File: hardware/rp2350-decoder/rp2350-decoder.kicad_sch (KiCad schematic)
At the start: 67 parts, among them J1 SWDIO, J2 SWCLK, J3 5052702412, Q1 DMN2991UDA-7B, Q2 DMN2991UDA-7B, Q3 NST847BPDP6T5G, Q4 NST847BPDP6T5G, Q5 DMN2991UDA-7B, Q6 DMN2991UDA-7B, Q7 DMN2991UDA-7B, Q8 DMN2991UDA-7B, SW1 BOOT, U1 NCS2220AMUT1G, U2 AP63203WU, U3 W25Q128JVPIQ, U4 RP2350A, U5 MAX98357AEWL+T, U6 MD9927, Y1 X252012MMB4SI

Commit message: chore: pcb cleanup
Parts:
- C2: Height 1.0 -> 0.9
- Y1: Frequency 12MHz -> (none)
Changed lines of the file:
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@@
 			)
 		)
-		(property "Datasheet" "https://lcsc.com/product-detail/Motor-Drivers_Shanghai-Mingda-Microelectronics-MD9927_C2684662.html"
+		(property "Datasheet" "https://www.lcsc.com/datasheet/lcsc_datasheet_2101111937_Shanghai-Mingda-Microelectronics-MD9927_C2684662.pdf"
 			(at 355.346 235.458 0)
 			(effects
@@
 			)
 		)
-		(property "Frequency" "12MHz"
-			(at 123.952 161.29 0)
-			(effects
-				(font
-					(size 1.27 1.27)
-				)
-			)
-		)
 		(pin "2"
 		)
@@
 			)
 		)
-		(property "Height" "1.0"
+		(property "Height" "0.9"
 			(at 74.93 54.61 0)
 			(effects

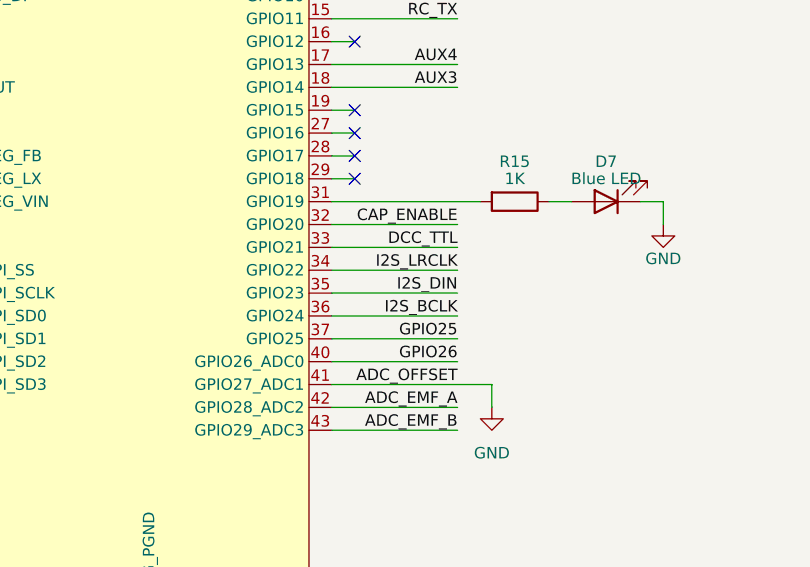
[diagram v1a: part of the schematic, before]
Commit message: chore: rearrange i2s pins for easier pio use
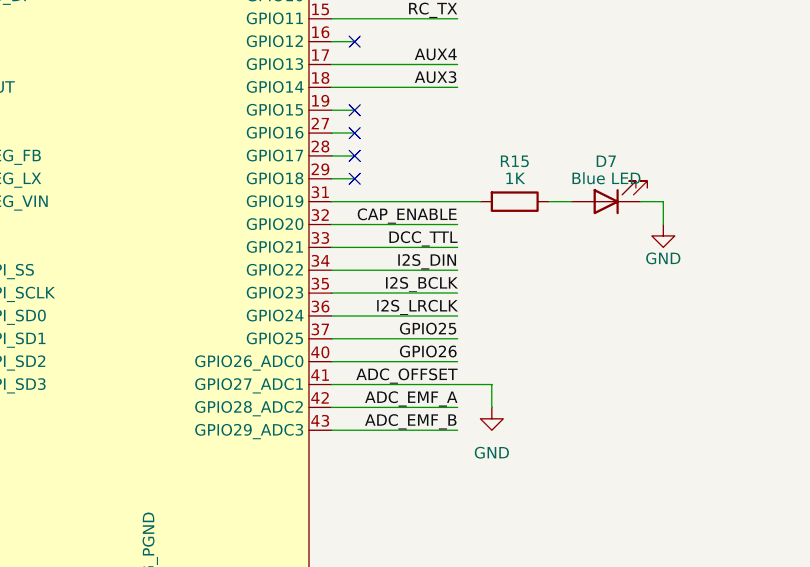
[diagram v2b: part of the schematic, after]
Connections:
- net I2S_BCLK: now also U4.35 (GPIO23); no longer U4.36 (GPIO24)
- net I2S_DIN: now also U4.34 (GPIO22); no longer U4.35 (GPIO23)
- net I2S_LRCLK: now also U4.36 (GPIO24); no longer U4.34 (GPIO22)
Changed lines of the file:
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@@
 	)
 	(label "I2S_BCLK"
-		(at 246.38 219.71 180)
+		(at 246.38 217.17 180)
 		(effects
 			(font
@@
 	)
 	(label "I2S_DIN"
-		(at 246.38 217.17 180)
+		(at 246.38 214.63 180)
 		(effects
 			(font
@@
 	)
 	(label "I2S_LRCLK"
-		(at 246.38 214.63 180)
-		(effects
-			(font
+		(at 246.38 219.71 180)
+		(effects
+			(font

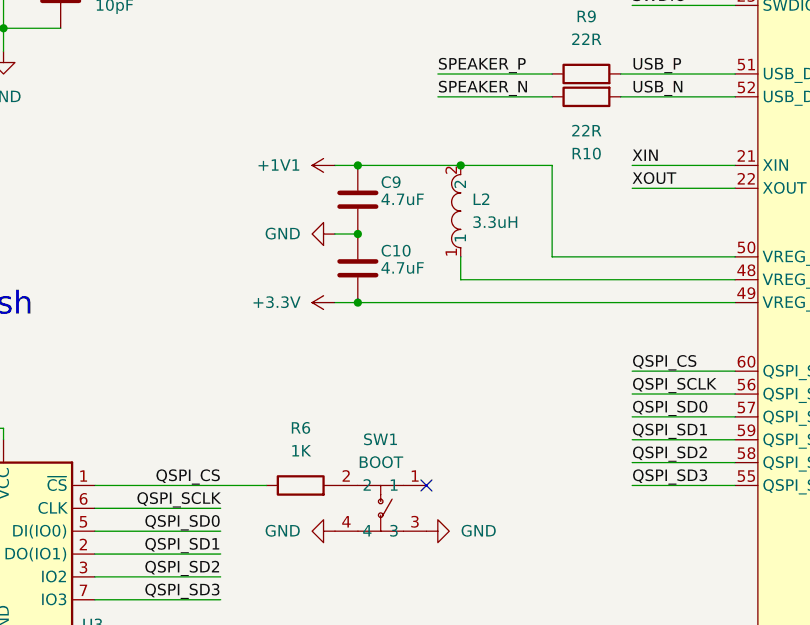
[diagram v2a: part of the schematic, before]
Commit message: chore: increase bootsel resistance
chore: add missing heights
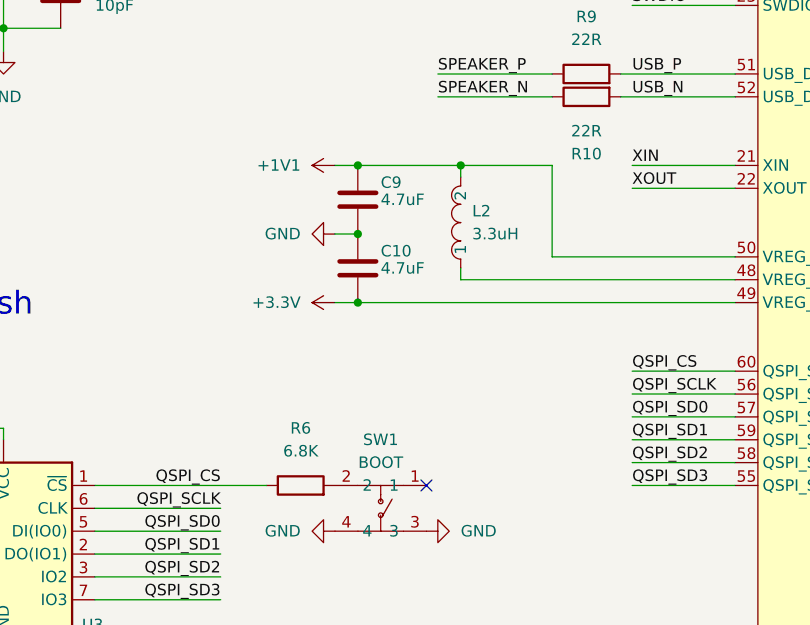
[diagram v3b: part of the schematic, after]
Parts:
- C14: Height 0.7 -> 0.55
- J1, J2: Height (none) -> 0
- L2: Height (none) -> 1.0; LCSC Part (none) -> C42411119
- Q3, Q4: Height (none) -> 0.4
- R10, R11, R13, R14, R5, R9: Height (none) -> 0.26
- R6: value 1K -> 6.8K; LCSC C270365 -> C423451
- U4: Height (none) -> 0.9
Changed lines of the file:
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@@
 	(wire
 		(pts
-			(xy 158.75 201.93) (xy 158.75 204.47)
+			(xy 158.75 203.2) (xy 158.75 204.47)
 		)
 		(stroke
@@
 	(wire
 		(pts
+			(xy 158.75 193.04) (xy 158.75 191.77)
+		)
+		(stroke
+			(width 0)
+			(type default)
+		)
+	)
+	(wire
+		(pts
 			(xy 232.41 204.47) (xy 234.95 204.47)
 		)
@@
 			)
 		)
+		(property "Height" "0.4"
+			(at 215.9 48.26 0)
+			(effects
+				(font
+					(size 1.27 1.27)
+				)
+				(hide yes)
+			)
+		)
 		(pin "2"
 		)
@@
 			)
 		)
+		(property "Height" "0.26"
+			(at 224.79 57.15 0)
+			(effects
+				(font
+					(size 1.27 1.27)
+				)
+				(hide yes)
+			)
+		)
 		(pin "1"
 		)
@@
 			)
 		)
+		(property "Height" "0.26"
+			(at 96.52 167.64 0)
+			(effects
+				(font
+					(size 1.27 1.27)
+				)
+				(hide yes)
+			)
+		)
 		(pin "1"
 		)
@@
 			)
 		)
+		(property "Height" "0.4"
+			(at 201.93 76.2 0)
+			(effects
+				(font
+					(size 1.27 1.27)
+				)
+				(hide yes)
+			)
+		)
 		(pin "2"
 		)
@@
 			)
 		)
+		(property "Height" "0.26"
+			(at 172.72 181.61 0)
+			(effects
+				(font
+					(size 1.27 1.27)
+				)
+				(hide yes)
+			)
+		)
 		(pin "2"
 		)
@@
 	(symbol
 		(lib_id "rp2350-decoder:AOTA-B201610S3R3-101-T")
-		(at 158.75 196.85 90)
+		(at 158.75 198.12 90)
 		(unit 1)
 		(exclude_from_sim no)
@@
 		(fields_autoplaced yes)
 		(property "Reference" "L2"
-			(at 160.02 195.5799 90)
+			(at 160.02 196.8499 90)
 			(effects
 				(font
@@
 		)
 		(property "Value" "3.3uH"
-			(at 160.02 198.1199 90)
+			(at 160.02 199.3899 90)
 			(effects
 				(font
@@
 		)
 		(property "Footprint" "rp2350-decoder:IND-SMD_L2.0-W1.6_AOTA-B201610S3R3-101-T"
-			(at 166.37 196.85 0)
+			(at 166.37 198.12 0)
 			(effects
 				(font
@@
 		)
 		(property "Datasheet" "https://jlcpcb.com/api/file/downloadByFileSystemAccessId/8567843503118221312"
-			(at 158.75 196.85 0)
+			(at 158.75 198.12 0)
 			(effects
 				(font
@@
 		)
 		(property "Description" ""
-			(at 158.75 196.85 0)
+			(at 158.75 198.12 0)
 			(effects
 				(font
@@
 		)
 		(property "LCSC" "C42411119"
-			(at 168.91 196.85 0)
+			(at 168.91 198.12 0)
+			(effects
+				(font
+					(size 1.27 1.27)
+				)
+				(hide yes)
+			)
+		)
+		(property "Height" "1.0"
+			(at 158.75 198.12 0)
+			(effects
+				(font
+					(size 1.27 1.27)
+				)
+				(hide yes)
+			)
+		)
+		(property "LCSC Part" "C42411119"
+			(at 168.91 198.12 0)
 			(effects
 				(font
@@
 			)
 		)
-		(property "Value" "1K"
+		(property "Value" "6.8K"
 			(at 140.97 223.52 90)
 			(effects
@@
 			)
 		)
-		(property "LCSC" "C270365"
+		(property "LCSC" "C423451"
 			(at 140.97 227.33 0)
 			(effects
@@
 			)
 		)
+		(property "Height" "0"
+			(at 160.02 154.94 0)
+			(effects
+				(font
+					(size 1.27 1.27)
+				)
+				(hide yes)
+			)
+		)
 		(pin "1"
 		)
@@
 			)
 		)
-		(property "Height" "0.7"
+		(property "Height" "0.55"
 			(at 236.22 140.97 0)
 			(effects
@@
 			)
 		)
+		(property "Height" "0.4"
+			(at 209.55 57.15 0)
+			(effects
+				(font
+					(size 1.27 1.27)
+				)
+				(hide yes)
+			)
+		)
 		(pin "2"
 		)
@@
 			)
 		)
+		(property "Height" "0.26"
+			(at 207.01 44.45 0)
+			(effects
+				(font
+					(size 1.27 1.27)
+				)
+				(hide yes)
+			)
+		)
 		(pin "2"
 		)
@@
 			)
 		)
+		(property "Height" "0.4"
+			(at 219.71 76.2 0)
+			(effects
+				(font
+					(size 1.27 1.27)
+				)
+				(hide yes)
+			)
+		)
 		(pin "2"
 		)
@@
 			)
 		)
+		(property "Height" "0.26"
+			(at 172.72 184.15 0)
+			(effects
+				(font
+					(size 1.27 1.27)
+				)
+				(hide yes)
+			)
+		)
 		(pin "2"
 		)
@@
 			)
 		)
+		(property "Height" "0"
+			(at 160.02 160.02 0)
+			(effects
+				(font
+					(size 1.27 1.27)
+				)
+				(hide yes)
+			)
+		)
 		(pin "1"
 		)
@@
 			)
 		)
+		(property "Height" "0.26"
+			(at 246.38 134.62 0)
+			(effects
+				(font
+					(size 1.27 1.27)
+				)
+				(hide yes)
+			)
+		)
 		(pin "2"
 		)
@@
 			(effects
 				(font
+					(size 1.27 1.27)
+				)
+				(hide yes)
+			)
+		)
+		(property "Height" "0.9"
+			(at 210.82 195.58 0)
+			(effects
+				(font

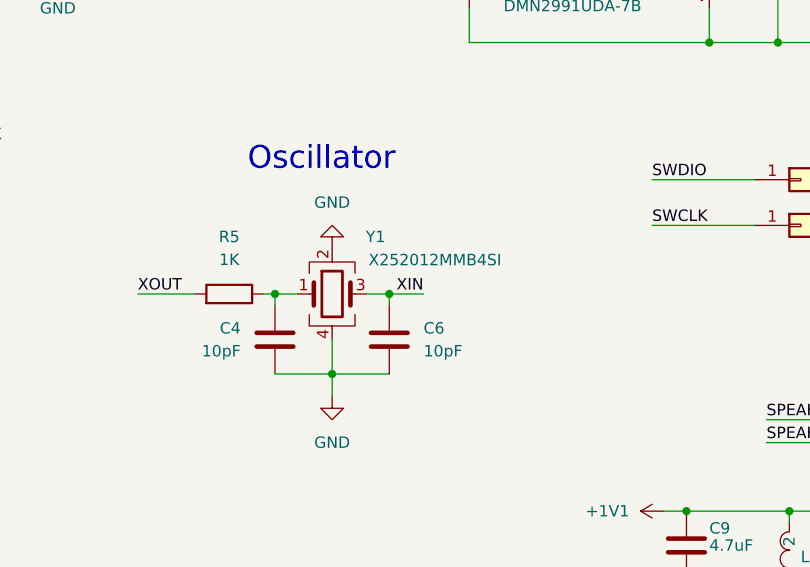
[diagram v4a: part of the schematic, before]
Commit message: fix: switch to recommended crystal
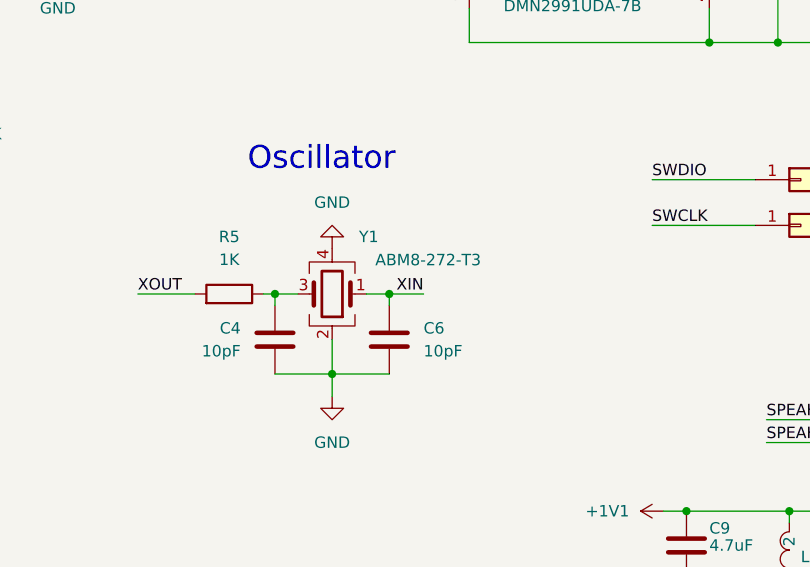
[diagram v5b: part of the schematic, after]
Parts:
- Y1: value X252012MMB4SI -> ABM8-272-T3; footprint Crystal:Crystal_SMD_2520-4Pin_2.5x2.0mm -> Crystal:Crystal_SMD_3225-4Pin_3.2x2.5mm; Height 0.65 -> 0.8; LCSC C2896601 -> C20625731
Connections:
- net XIN: now also Y1.1; no longer Y1.3
- net at C4.1, R5.1: now also Y1.3; no longer Y1.1
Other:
- moved on the sheet: Y1
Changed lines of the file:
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@@
 	(symbol
 		(lib_id "Device:Crystal_GND24")
-		(at 107.95 167.64 0)
+		(at 107.95 167.64 180)
 		(unit 1)
 		(exclude_from_sim no)
@@
 		(dnp no)
 		(property "Reference" "Y1"
-			(at 112.776 161.29 0)
+			(at 112.014 161.29 0)
 			(effects
 				(font
@@
 			)
 		)
-		(property "Value" "X252012MMB4SI"
-			(at 119.38 163.8614 0)
+		(property "Value" "ABM8-272-T3"
+			(at 118.618 163.8614 0)
 			(effects
 				(font
@@
 			)
 		)
-		(property "Footprint" "Crystal:Crystal_SMD_2520-4Pin_2.5x2.0mm"
+		(property "Footprint" "Crystal:Crystal_SMD_3225-4Pin_3.2x2.5mm"
 			(at 107.95 167.64 0)
 			(effects
@@
 			)
 		)
-		(property "Datasheet" "https://wmsc.lcsc.com/wmsc/upload/file/pdf/v2/lcsc/2403291506_YXC-Crystal-Oscillators-X252012MMB4SI-24_C2896601.pdf"
+		(property "Datasheet" "https://jlcpcb.com/api/file/downloadByFileSystemAccessId/8559470777180311552"
 			(at 107.95 167.64 0)
 			(effects
@@
 			)
 		)
-		(property "LCSC" "C2896601"
+		(property "LCSC" "C20625731"
 			(at 107.95 167.64 0)
 			(effects
@@
 			)
 		)
-		(property "Height" "0.65"
+		(property "Height" "0.8"
 			(at 107.95 167.64 0)
 			(effects
